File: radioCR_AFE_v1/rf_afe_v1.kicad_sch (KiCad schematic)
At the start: 39 parts, among them J1 Conn_Coaxial, J2 Conn_Coaxial, U1 PHA-13LN, U2 BSF108+, U3 PHA-13LN, U4 RBP188, U5 PSA8A+, U6 TCBT-6G+

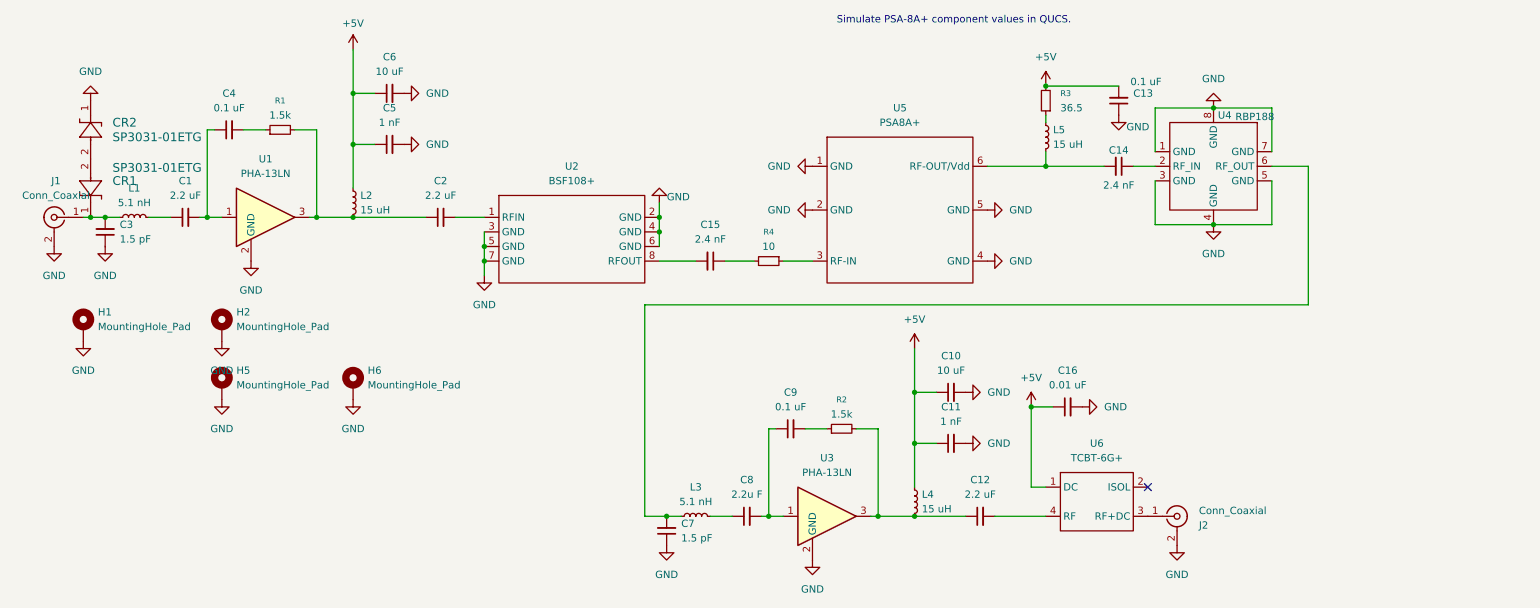
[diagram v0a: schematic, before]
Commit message: attenuator added to schematic and PCB
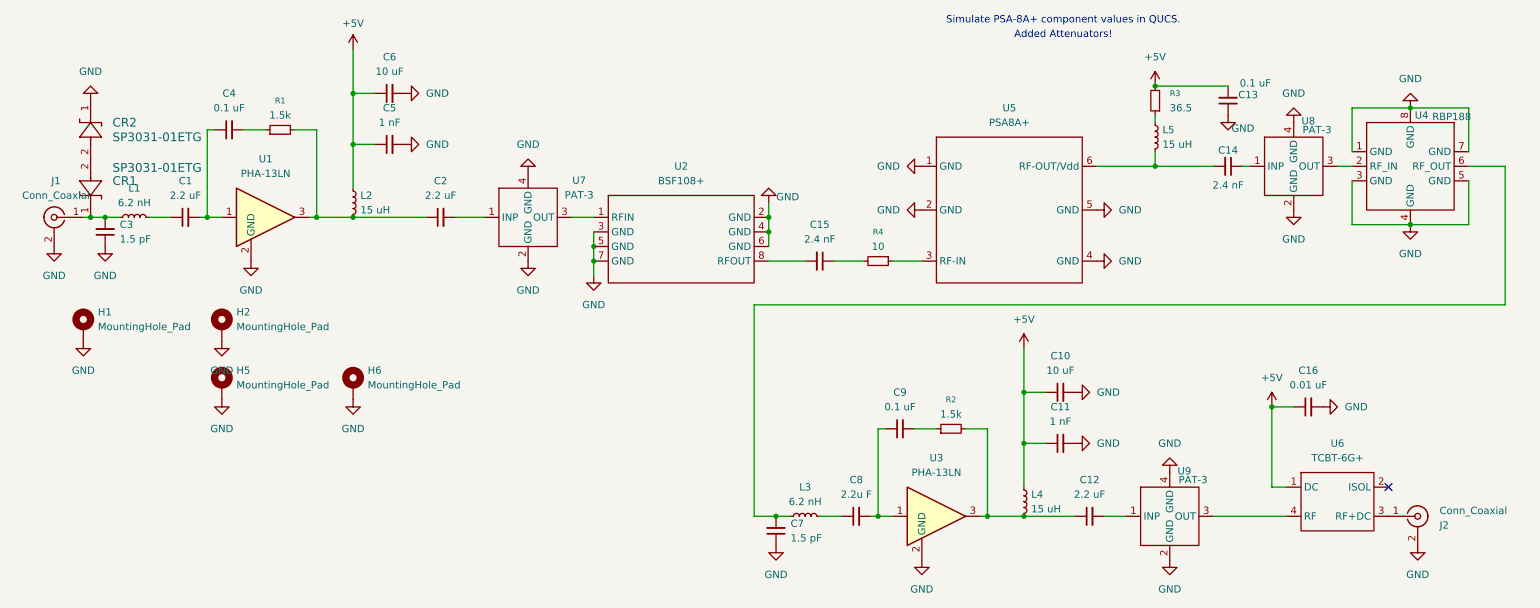
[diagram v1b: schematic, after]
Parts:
- added U7, U8, U9: PAT-3, minickts_kicad:PAT-3+, symbol minicircuits:PAT-3
- L1, L3: value 5.1 nH -> 6.2 nH
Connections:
- net GND: now also U7.2 (GND), U7.4 (GND), U8.2 (GND), U8.4 (GND), U9.2 (GND), U9.4 (GND)
- net at U2.1 (RFIN): now also U7.3 (OUT); no longer C2.2
- net at C12.2: now also U9.1 (INP); no longer U6.4 (RF)
- net at C14.1: now also U8.1 (INP); no longer U4.2 (RF_IN)
- new net: U6.4 (RF), U9.3 (OUT)
- new net: U4.2 (RF_IN), U8.3 (OUT)
- new net: C2.2, U7.1 (INP)
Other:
- note added: "Added Attenuators!"
- moved on the sheet: C10, C11, C12, C13, C14, C15, C16, C7, C8, C9, J2, L3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

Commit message: updated C1 footprint, regen bom
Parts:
- C1: footprint Capacitor_SMD:C_0603_1608Metric -> Capacitor_SMD:C_0805_2012Metric
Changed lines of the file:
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@@
 			)
 		)
-		(property "Datasheet" ""
+		(property "Datasheet" "PAT-3+"
 			(at 214.63 135.89 0)
 			(effects
@@
 			)
 		)
-		(property "Datasheet" "https://www.minicircuits.com/pdfs/BSF-108+.pdf"
+		(property "Datasheet" "BSF-108+"
 			(at 129.54 87.63 0)
 			(effects
@@
 			)
 		)
-		(property "Datasheet" "~"
+		(property "Datasheet" "MC002126"
 			(at 257.81 135.89 0)
 			(effects
@@
 			)
 		)
-		(property "Footprint" "Capacitor_SMD:C_0603_1608Metric"
+		(property "Footprint" "Capacitor_SMD:C_0805_2012Metric"
 			(at 43.18 83.82 0)
 			(effects
@@
 			)
 		)
-		(property "Datasheet" "https://www.mouser.in/ProductDetail/Littelfuse/SP3031-01ETG?qs=B%2FZyIADl9o%252B%2FfpJwZJPmLg%3D%3D"
+		(property "Datasheet" "SP3031-01ETG"
 			(at 26.67 73.66 0)
 			(effects
@@
 			)
 		)
-		(property "Datasheet" ""
+		(property "Datasheet" "PAT-3+"
 			(at 236.22 74.93 0)
 			(effects
@@
 			)
 		)
-		(property "Datasheet" "https://www.minicircuits.com/pdfs/RBP-188+.pdf"
+		(property "Datasheet" "RBP188"
 			(at 256.54 74.93 0)
 			(effects
@@
 			)
 		)
-		(property "Datasheet" ""
+		(property "Datasheet" "PAT-3+"
 			(at 102.87 83.82 0)
 			(effects
@@
 			)
 		)
-		(property "Datasheet" "https://www.minicircuits.com/pdfs/PSA-8A+.pdf"
+		(property "Datasheet" "PSA8A+"
 			(at 186.69 82.55 0)
 			(effects
@@
 			)
 		)
-		(property "Datasheet" "https://www.mouser.in/ProductDetail/Littelfuse/SP3031-01ETG?qs=B%2FZyIADl9o%252B%2FfpJwZJPmLg%3D%3D"
+		(property "Datasheet" "SP3031-01ETG"
 			(at 26.67 73.66 0)
 			(effects
@@
 			)
 		)
-		(property "Datasheet" "~"
+		(property "Datasheet" "MC002126"
 			(at 20.32 83.82 0)
 			(effects
@@
 			)
 		)
-		(property "Datasheet" "https://www.minicircuits.com/pdfs/PHA-13LN+.pdf"
+		(property "Datasheet" "PHA-13LN+"
 			(at 173.99 135.89 0)
 			(effects
@@
 			)
 		)
-		(property "Datasheet" "https://www.minicircuits.com/pdfs/PHA-13LN+.pdf"
+		(property "Datasheet" "PHA-13LN+"
 			(at 57.15 83.82 0)
 			(effects
@@
 			)
 		)
-		(property "Datasheet" "https://www.minicircuits.com/pdfs/TCBT-6G+.pdf"
+		(property "Datasheet" "TCBT-6G+"
 			(at 243.84 133.35 0)
 			(effects
